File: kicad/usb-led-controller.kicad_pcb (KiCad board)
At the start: 2 copper layers, 70 x 50 mm, 37 parts, among them J1 SWD, J2 PWR, J3 USB, J4 PWM_0, J5 PWM_1, J6 WS2812_0, J7 WS2812_1, Q1 NVS4409N, Q2 NVS4409N, Q3 NVS4409N, Q4 NVS4409N, Q5 NVS4409N, Q6 NVS4409N, U1 SN74LV1T04, U2 SN74LV1T04, U3 STM32L052K6Ux, U4 MIC5501-XYM5, U5 USBLC6

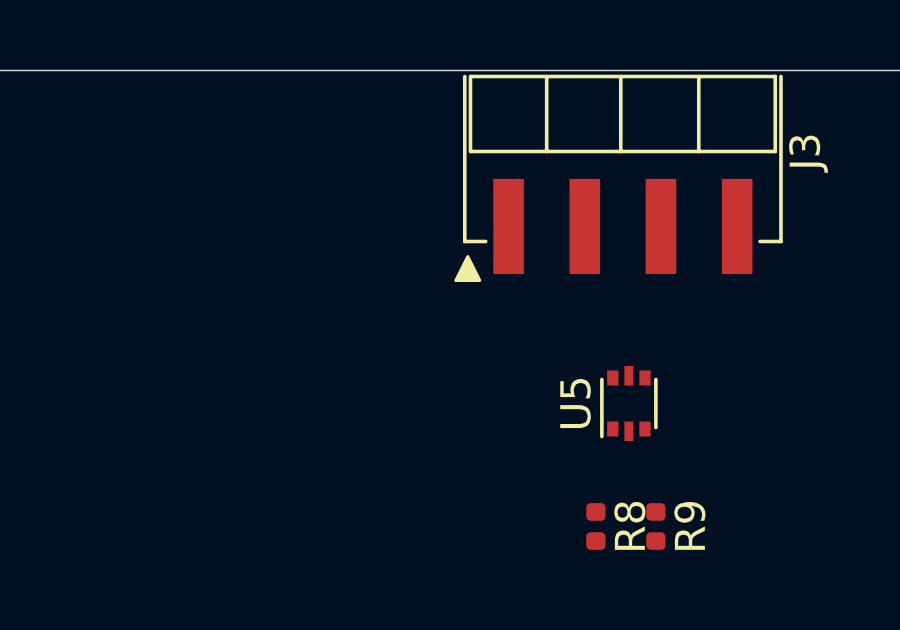
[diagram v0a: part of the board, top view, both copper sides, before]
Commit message: Configuring 4-layer board stackup with netclasses
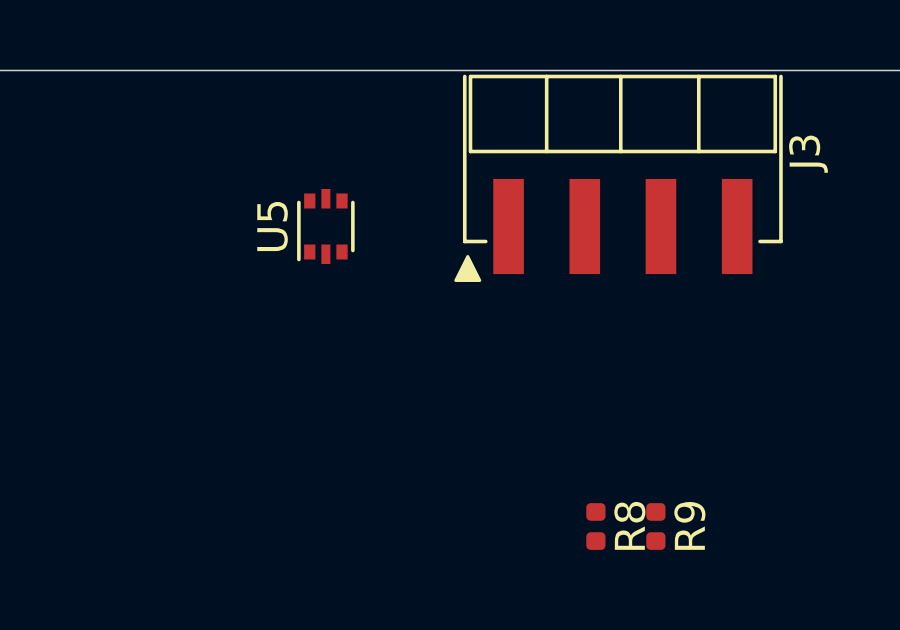
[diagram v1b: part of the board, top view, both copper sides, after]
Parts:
- moved U5 11.7 mm to (174.3, 105.2)
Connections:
- net Net-(R3-Pad1) renamed /REG_3V3_EN
- U5 pad 1: /USB_D_TVS- -> /USB_D_TVS+
- U5 pad 3: /USB_D_TVS+ -> /USB_D_TVS-
- U5 pad 4: /USB_D+ -> /USB_D-
- U5 pad 6: /USB_D- -> /USB_D+
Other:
- copper layers 2 -> 4
- net class Default: trace_width 0.25 -> 0.254
- net class Power added: clearance 0.2, trace_width 0.508, via_dia 0.8, via_drill 0.4
- net class USB added: clearance 0.2, trace_width 0.254, via_dia 0.45, via_drill 0.2
- rule trace_min: 0.2 -> 0.127
- rule via_min_drill: 0.3 -> 0.2
- rule via_min_size: 0.4 -> 0.45

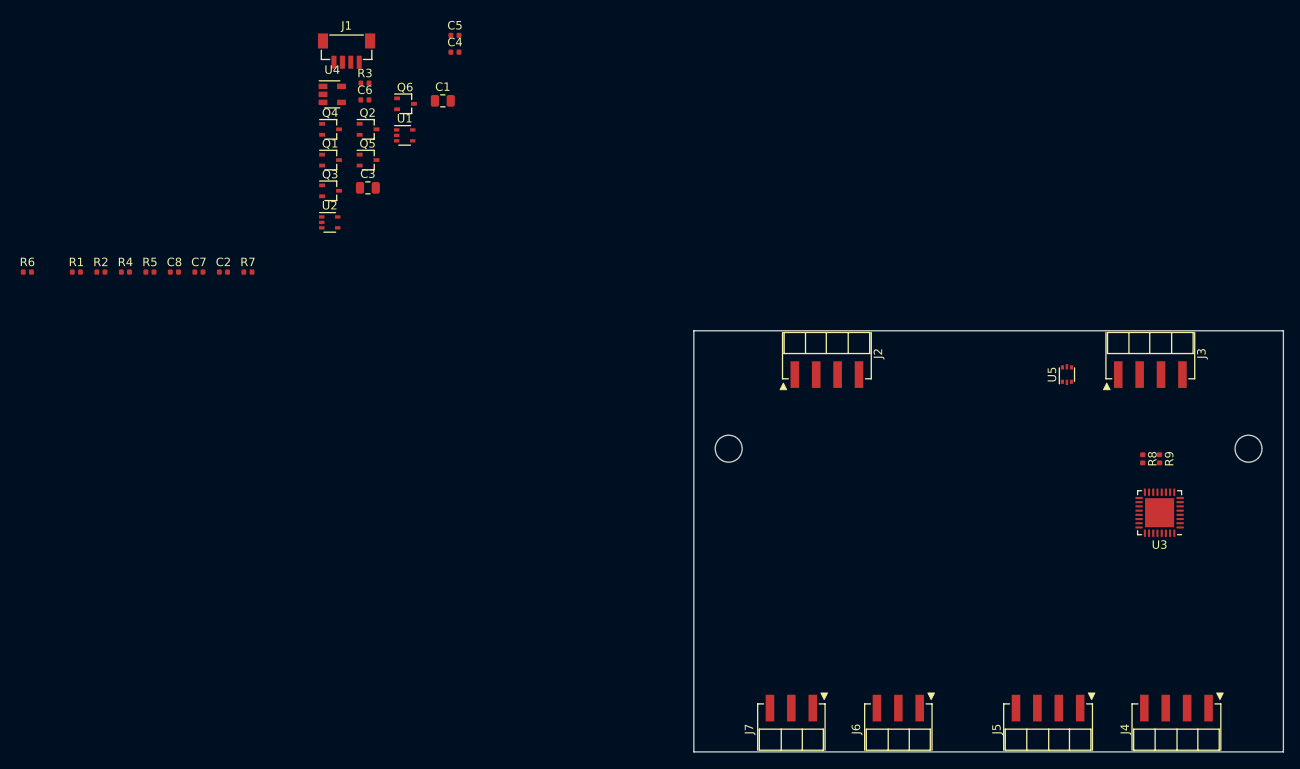
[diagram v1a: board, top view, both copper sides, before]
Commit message: Changing microcontroller and redoing WS2812 control
The QFN package required VIPPO to be easily soldered. I could
probably have done it without plating-over, but it still requires the
heat gun and it is currently broken.

The family was downgraded to an ST32F042, which is a little clunkier
than the STM32L052 family. It also doesn't have very accessible UARTs
when USB is being used, so I swapped out the level shifters to tri-state
ones and used the remaining GPIOs as enables.
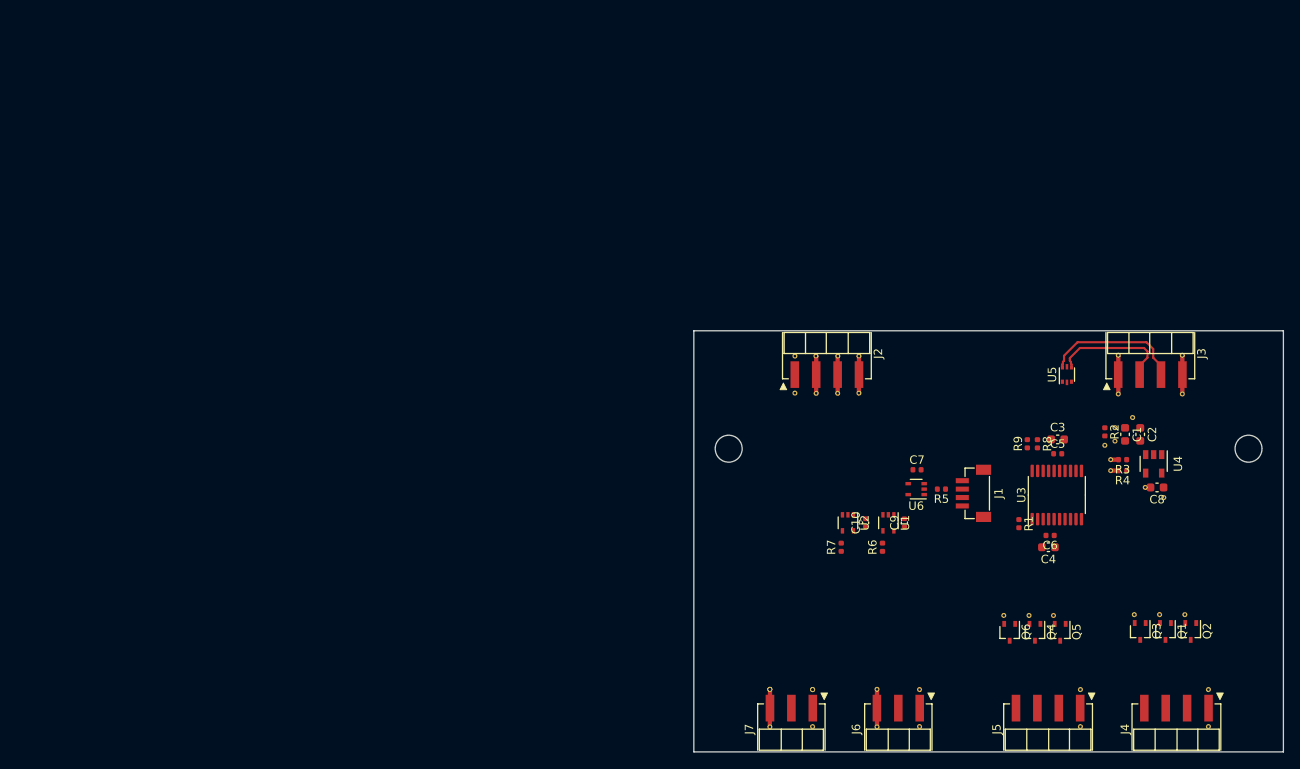
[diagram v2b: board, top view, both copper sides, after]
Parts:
- added C10: 0u1, Capacitor_SMD:C_0402_1005Metric, F.Cu at (150.4, 122.8)
- added C9: 0u1, Capacitor_SMD:C_0402_1005Metric, F.Cu at (155.0, 122.8)
- added REF**: VIA-0.3_0.6-TENT, usb-led-controller:VIA-0.3_0.6-TENT, F.Cu at (188.3, 133.7)
- added REF**: VIA-0.3_0.6-TENT, usb-led-controller:VIA-0.3_0.6-TENT, F.Cu at (156.8, 147.0)
- added REF**: VIA-0.3_0.6-TENT, usb-led-controller:VIA-0.3_0.6-TENT, F.Cu at (156.8, 142.6)
- added REF**: VIA-0.3_0.6-TENT, usb-led-controller:VIA-0.3_0.6-TENT, F.Cu at (191.1, 147.0)
- added REF**: VIA-0.3_0.6-TENT, usb-led-controller:VIA-0.3_0.6-TENT, F.Cu at (191.1, 142.6)
- added REF**: VIA-0.3_0.6-TENT, usb-led-controller:VIA-0.3_0.6-TENT, F.Cu at (175.9, 147.0)
- added REF**: VIA-0.3_0.6-TENT, usb-led-controller:VIA-0.3_0.6-TENT, F.Cu at (175.9, 142.6)
- added REF**: VIA-0.3_0.6-TENT, usb-led-controller:VIA-0.3_0.6-TENT, F.Cu at (142.0, 103.0)
- added REF**: VIA-0.3_0.6-TENT, usb-led-controller:VIA-0.3_0.6-TENT, F.Cu at (185.8, 119.8)
- added REF**: VIA-0.3_0.6-TENT, usb-led-controller:VIA-0.3_0.6-TENT, F.Cu at (142.0, 107.4)
- added REF**: VIA-0.3_0.6-TENT, usb-led-controller:VIA-0.3_0.6-TENT, F.Cu at (182.1, 110.3)
- added REF**: VIA-0.3_0.6-TENT, usb-led-controller:VIA-0.3_0.6-TENT, F.Cu at (185.3, 133.7)
- added REF**: VIA-0.3_0.6-TENT, usb-led-controller:VIA-0.3_0.6-TENT, F.Cu at (180.0, 111.5)
- added REF**: VIA-0.3_0.6-TENT, usb-led-controller:VIA-0.3_0.6-TENT, F.Cu at (183.6, 118.6)
- added REF**: VIA-0.3_0.6-TENT, usb-led-controller:VIA-0.3_0.6-TENT, F.Cu at (180.0, 113.1)
- added REF**: VIA-0.3_0.6-TENT, usb-led-controller:VIA-0.3_0.6-TENT, F.Cu at (178.8, 113.6)
- added REF**: VIA-0.3_0.6-TENT, usb-led-controller:VIA-0.3_0.6-TENT, F.Cu at (144.5, 103.0)
- added REF**: VIA-0.3_0.6-TENT, usb-led-controller:VIA-0.3_0.6-TENT, F.Cu at (147.1, 103.0)
- added REF**: VIA-0.3_0.6-TENT, usb-led-controller:VIA-0.3_0.6-TENT, F.Cu at (149.6, 103.0)
- added REF**: VIA-0.3_0.6-TENT, usb-led-controller:VIA-0.3_0.6-TENT, F.Cu at (149.6, 107.4)
- added REF**: VIA-0.3_0.6-TENT, usb-led-controller:VIA-0.3_0.6-TENT, F.Cu at (147.1, 107.4)
- added REF**: VIA-0.3_0.6-TENT, usb-led-controller:VIA-0.3_0.6-TENT, F.Cu at (144.5, 107.4)
- added REF**: VIA-0.3_0.6-TENT, usb-led-controller:VIA-0.3_0.6-TENT, F.Cu at (182.3, 133.7)
- added REF** (x2): VIA-0.3_0.6-TENT, usb-led-controller:VIA-0.3_0.6-TENT, F.Cu at (139.0, 142.6)
- added REF**: VIA-0.3_0.6-TENT, usb-led-controller:VIA-0.3_0.6-TENT, F.Cu at (139.0, 147.0)
- added REF**: VIA-0.3_0.6-TENT, usb-led-controller:VIA-0.3_0.6-TENT, F.Cu at (151.8, 147.0)
- added REF**: VIA-0.3_0.6-TENT, usb-led-controller:VIA-0.3_0.6-TENT, F.Cu at (151.8, 142.6)
- added REF**: VIA-0.3_0.6-TENT, usb-led-controller:VIA-0.3_0.6-TENT, F.Cu at (179.5, 116.6)
- added REF**: VIA-0.3_0.6-TENT, usb-led-controller:VIA-0.3_0.6-TENT, F.Cu at (179.5, 115.3)
- added REF**: VIA-0.3_0.6-TENT, usb-led-controller:VIA-0.3_0.6-TENT, F.Cu at (188.0, 107.5)
- added REF**: VIA-0.3_0.6-TENT, usb-led-controller:VIA-0.3_0.6-TENT, F.Cu at (188.0, 102.9)
- added REF**: VIA-0.3_0.6-TENT, usb-led-controller:VIA-0.3_0.6-TENT, F.Cu at (180.4, 102.9)
- added REF**: VIA-0.3_0.6-TENT, usb-led-controller:VIA-0.3_0.6-TENT, F.Cu at (172.7, 133.8)
- added REF**: VIA-0.3_0.6-TENT, usb-led-controller:VIA-0.3_0.6-TENT, F.Cu at (180.4, 107.5)
- added REF**: VIA-0.3_0.6-TENT, usb-led-controller:VIA-0.3_0.6-TENT, F.Cu at (169.8, 133.8)
- added REF**: VIA-0.3_0.6-TENT, usb-led-controller:VIA-0.3_0.6-TENT, F.Cu at (166.8, 133.8)
- added REF** (x2): VIA-0.3_0.6-TENT, usb-led-controller:VIA-0.3_0.6-TENT, F.Cu at (144.1, 142.6)
- added REF**: VIA-0.3_0.6-TENT, usb-led-controller:VIA-0.3_0.6-TENT, F.Cu at (144.1, 147.0)
- added U6: SN74LVC1G04, Package_TO_SOT_SMD:SOT-353_SC-70-5, F.Cu at (156.4, 118.8)
- C1: footprint Capacitor_SMD:C_0805_2012Metric -> Capacitor_SMD:C_0603_1608Metric
- C2, C4, C8: footprint Capacitor_SMD:C_0402_1005Metric -> Capacitor_SMD:C_0603_1608Metric
- C3: value 10u -> 4u7; footprint Capacitor_SMD:C_0805_2012Metric -> Capacitor_SMD:C_0603_1608Metric
- C6: value 0u1 -> 0u01
- U1, U2: value SN74LV1T04 -> SN74LV1T125
- U3: value STM32L052K6Ux -> STM32F042F6Px; footprint Package_DFN_QFN:QFN-32-1EP_5x5mm_P0.5mm_EP3.45x3.45mm -> Package_SO:TSSOP-20_4.4x6.5mm_P0.65mm
- moved R4 120.7 mm to (180.9, 116.6), turned to 180 degrees
- moved R2 120.7 mm to (178.8, 112.0), turned to 270 degrees
- moved C8 119.4 mm to (185.0, 118.6), turned to 180 degrees
- moved R1 115.8 mm to (168.6, 122.9), turned to 270 degrees
- moved Q2 114.4 mm to (189.0, 135.7), turned to 270 degrees
- moved Q1 113.8 mm to (186.0, 135.7), turned to 270 degrees
- moved C2 110.5 mm to (183.0, 112.3), turned to 270 degrees
- moved Q3 109.4 mm to (183.0, 135.7), turned to 270 degrees
- moved U4 106.9 mm to (184.6, 115.8), turned to 270 degrees
- moved R6 106.7 mm to (152.4, 125.7), turned to 90 degrees
- moved Q4 102.8 mm to (170.5, 135.8), turned to 270 degrees
- moved R3 100.4 mm to (180.9, 115.3), turned to 180 degrees
- moved Q5 99.5 mm to (173.5, 135.8), turned to 270 degrees
- moved R5 97.4 mm to (159.4, 118.8), turned to 180 degrees
- moved C6 96.4 mm to (172.3, 124.3), turned to 180 degrees
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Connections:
- R5 pad 2: /WS2812_1_DATA_IO -> /WS2812_DATA
- U1 pad 1: (no net) -> /WS2812_0_~OE
- U1 pad 2: /WS2812_0_DATA_IO -> /WS2812_DATA_INV
- U2 pad 1: (no net) -> /WS2812_1_~OE
- U2 pad 2: /WS2812_1_DATA_IO -> /WS2812_DATA_INV
- U3 pad 1: +3V3 -> /BOOT0
- U3 pad 10: Net-(U3-Pad10) -> /WS2812_0_~OE
- U3 pad 11: Net-(U3-Pad11) -> /WS2812_1_~OE
- U3 pad 15: Net-(U3-Pad15) -> GND
- U3 pad 16: Net-(U3-Pad16) -> +3V3
- U3 pad 17: +3V3 -> /USB_D_R-
- U3 pad 18: Net-(U3-Pad18) -> /USB_D_R+
- U3 pad 19: /WS2812_0_DATA_IO -> /SWDIO
- U3 pad 20: Net-(U3-Pad20) -> /SWCLK
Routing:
- net GND: track 0.00 -> 27.7 mm
- net /USB_D+: track 0.00 -> 16.5 mm
- net /USB_D-: track 0.00 -> 14.2 mm
- net +5V: track 0.00 -> 5.52 mm
- added copper zone on In1.Cu, net GND

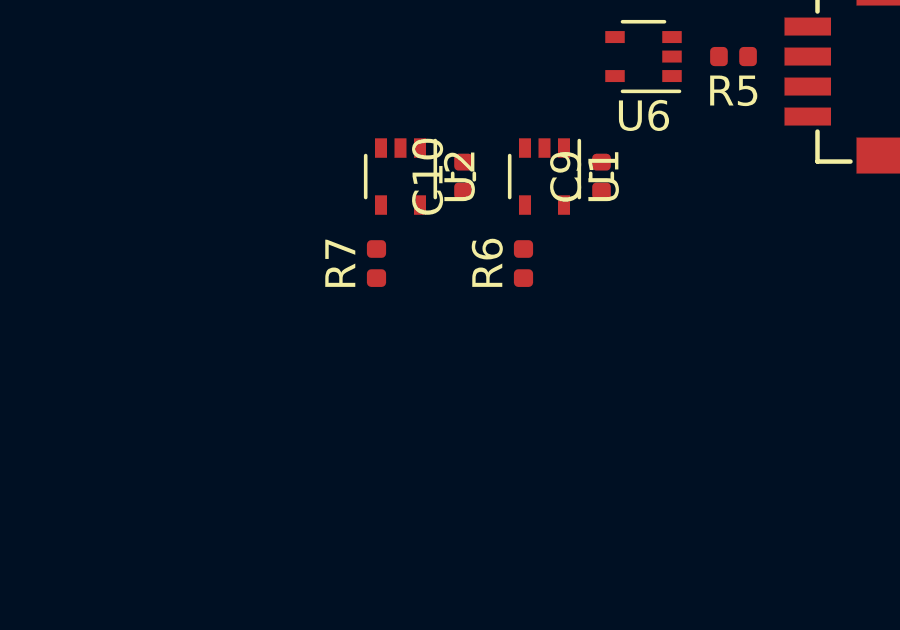
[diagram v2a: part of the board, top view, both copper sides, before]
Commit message: Adding pulldowns on WS2812 outputs
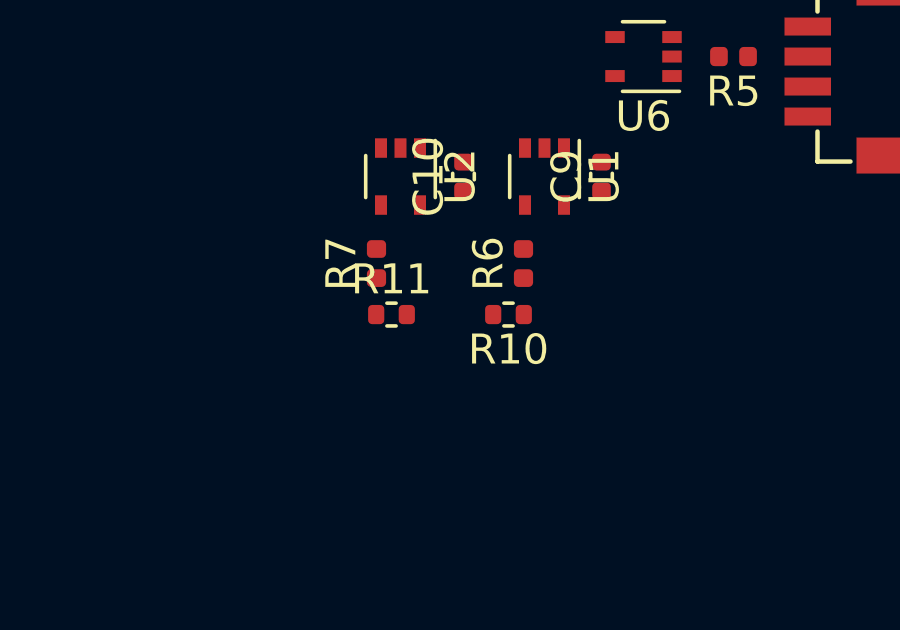
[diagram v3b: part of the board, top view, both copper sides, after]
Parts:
- added R10: 10K, Resistor_SMD:R_0402_1005Metric, F.Cu at (151.9, 127.4)
- added R11: 10K, Resistor_SMD:R_0402_1005Metric, F.Cu at (148.0, 127.4)
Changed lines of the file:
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@@
     (tracks 52)
     (zones 0)
-    (modules 80)
+    (modules 82)
     (nets 39)
   )
@@
     (add_net /USB_D_TVS-)
   )
+  (module Resistor_SMD:R_0402_1005Metric (layer F.Cu)
+    (at 148 127.4)
+    (descr "Resistor SMD 0402 (1005 Metric), square (rectangular) end terminal, IPC_7351 nominal, (Body size source: IPC-SM-782 page 72, https://www.pcb-3d.com/wordpress/wp-content/uploads/ipc-sm-782a_amendment_1_and_2.pdf), generated with kicad-footprint-generator")
+    (tags resistor)
+    (attr smd)
+    (fp_text reference R11 (at 0 -1.17) (layer F.SilkS)
+      (effects (font (size 1 1) (thickness 0.15)))
+    )
+    (fp_text value 10K (at 0 1.17) (layer F.Fab)
+      (effects (font (size 1 1) (thickness 0.15)))
+    )
+    (fp_text user %R (at 0 0) (layer F.Fab)
+      (effects (font (size 0.26 0.26) (thickness 0.04)))
+    )
+    (fp_line (start -0.525 0.27) (end -0.525 -0.27) (layer F.Fab) (width 0.1))
+    (fp_line (start -0.525 -0.27) (end 0.525 -0.27) (layer F.Fab) (width 0.1))
+    (fp_line (start 0.525 -0.27) (end 0.525 0.27) (layer F.Fab) (width 0.1))
+    (fp_line (start 0.525 0.27) (end -0.525 0.27) (layer F.Fab) (width 0.1))
+    (fp_line (start -0.153641 -0.38) (end 0.153641 -0.38) (layer F.SilkS) (width 0.12))
+    (fp_line (start -0.153641 0.38) (end 0.153641 0.38) (layer F.SilkS) (width 0.12))
+    (fp_line (start -0.93 0.47) (end -0.93 -0.47) (layer F.CrtYd) (width 0.05))
+    (fp_line (start -0.93 -0.47) (end 0.93 -0.47) (layer F.CrtYd) (width 0.05))
+    (fp_line (start 0.93 -0.47) (end 0.93 0.47) (layer F.CrtYd) (width 0.05))
+    (fp_line (start 0.93 0.47) (end -0.93 0.47) (layer F.CrtYd) (width 0.05))
+    (pad 2 smd roundrect (at 0.51 0) (size 0.54 0.64) (layers F.Cu F.Paste F.Mask) (roundrect_rratio 0.25)
+      (net 1 GND))
+    (pad 1 smd roundrect (at -0.51 0) (size 0.54 0.64) (layers F.Cu F.Paste F.Mask) (roundrect_rratio 0.25)
+      (net 26 /WS2812_1_DATA_R))
+    (model ${KISYS3DMOD}/Resistor_SMD.3dshapes/R_0402_1005Metric.wrl
+      (at (xyz 0 0 0))
+      (scale (xyz 1 1 1))
+      (rotate (xyz 0 0 0))
+    )
+  )
+  (module Resistor_SMD:R_0402_1005Metric (layer F.Cu)
+    (at 151.9 127.4 180)
+    (descr "Resistor SMD 0402 (1005 Metric), square (rectangular) end terminal, IPC_7351 nominal, (Body size source: IPC-SM-782 page 72, https://www.pcb-3d.com/wordpress/wp-content/uploads/ipc-sm-782a_amendment_1_and_2.pdf), generated with kicad-footprint-generator")
+    (tags resistor)
+    (attr smd)
+    (fp_text reference R10 (at 0 -1.17) (layer F.SilkS)
+      (effects (font (size 1 1) (thickness 0.15)))
+    )
+    (fp_text value 10K (at 0 1.17) (layer F.Fab)
+      (effects (font (size 1 1) (thickness 0.15)))
+    )
+    (fp_text user %R (at 0 0) (layer F.Fab)
+      (effects (font (size 0.26 0.26) (thickness 0.04)))
+    )
+    (fp_line (start -0.525 0.27) (end -0.525 -0.27) (layer F.Fab) (width 0.1))
+    (fp_line (start -0.525 -0.27) (end 0.525 -0.27) (layer F.Fab) (width 0.1))
+    (fp_line (start 0.525 -0.27) (end 0.525 0.27) (layer F.Fab) (width 0.1))
+    (fp_line (start 0.525 0.27) (end -0.525 0.27) (layer F.Fab) (width 0.1))
+    (fp_line (start -0.153641 -0.38) (end 0.153641 -0.38) (layer F.SilkS) (width 0.12))
+    (fp_line (start -0.153641 0.38) (end 0.153641 0.38) (layer F.SilkS) (width 0.12))
+    (fp_line (start -0.93 0.47) (end -0.93 -0.47) (layer F.CrtYd) (width 0.05))
+    (fp_line (start -0.93 -0.47) (end 0.93 -0.47) (layer F.CrtYd) (width 0.05))
+    (fp_line (start 0.93 -0.47) (end 0.93 0.47) (layer F.CrtYd) (width 0.05))
+    (fp_line (start 0.93 0.47) (end -0.93 0.47) (layer F.CrtYd) (width 0.05))
+    (pad 2 smd roundrect (at 0.51 0 180) (size 0.54 0.64) (layers F.Cu F.Paste F.Mask) (roundrect_rratio 0.25)
+      (net 1 GND))
+    (pad 1 smd roundrect (at -0.51 0 180) (size 0.54 0.64) (layers F.Cu F.Paste F.Mask) (roundrect_rratio 0.25)
+      (net 16 /WS2812_0_DATA))
+    (model ${KISYS3DMOD}/Resistor_SMD.3dshapes/R_0402_1005Metric.wrl
+      (at (xyz 0 0 0))
+      (scale (xyz 1 1 1))
+      (rotate (xyz 0 0 0))
+    )
+  )
   (module usb-led-controller:VIA-0.3_0.6-TENT locked (layer F.Cu)
